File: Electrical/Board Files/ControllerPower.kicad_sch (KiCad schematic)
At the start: 42 parts, among them J1 Conn_01x02_Female, Q1 PJA3411, Q2 PJA3411, SW11 SW_DIP_x01, U1 TPS63020, U2 BQ25050DQCR

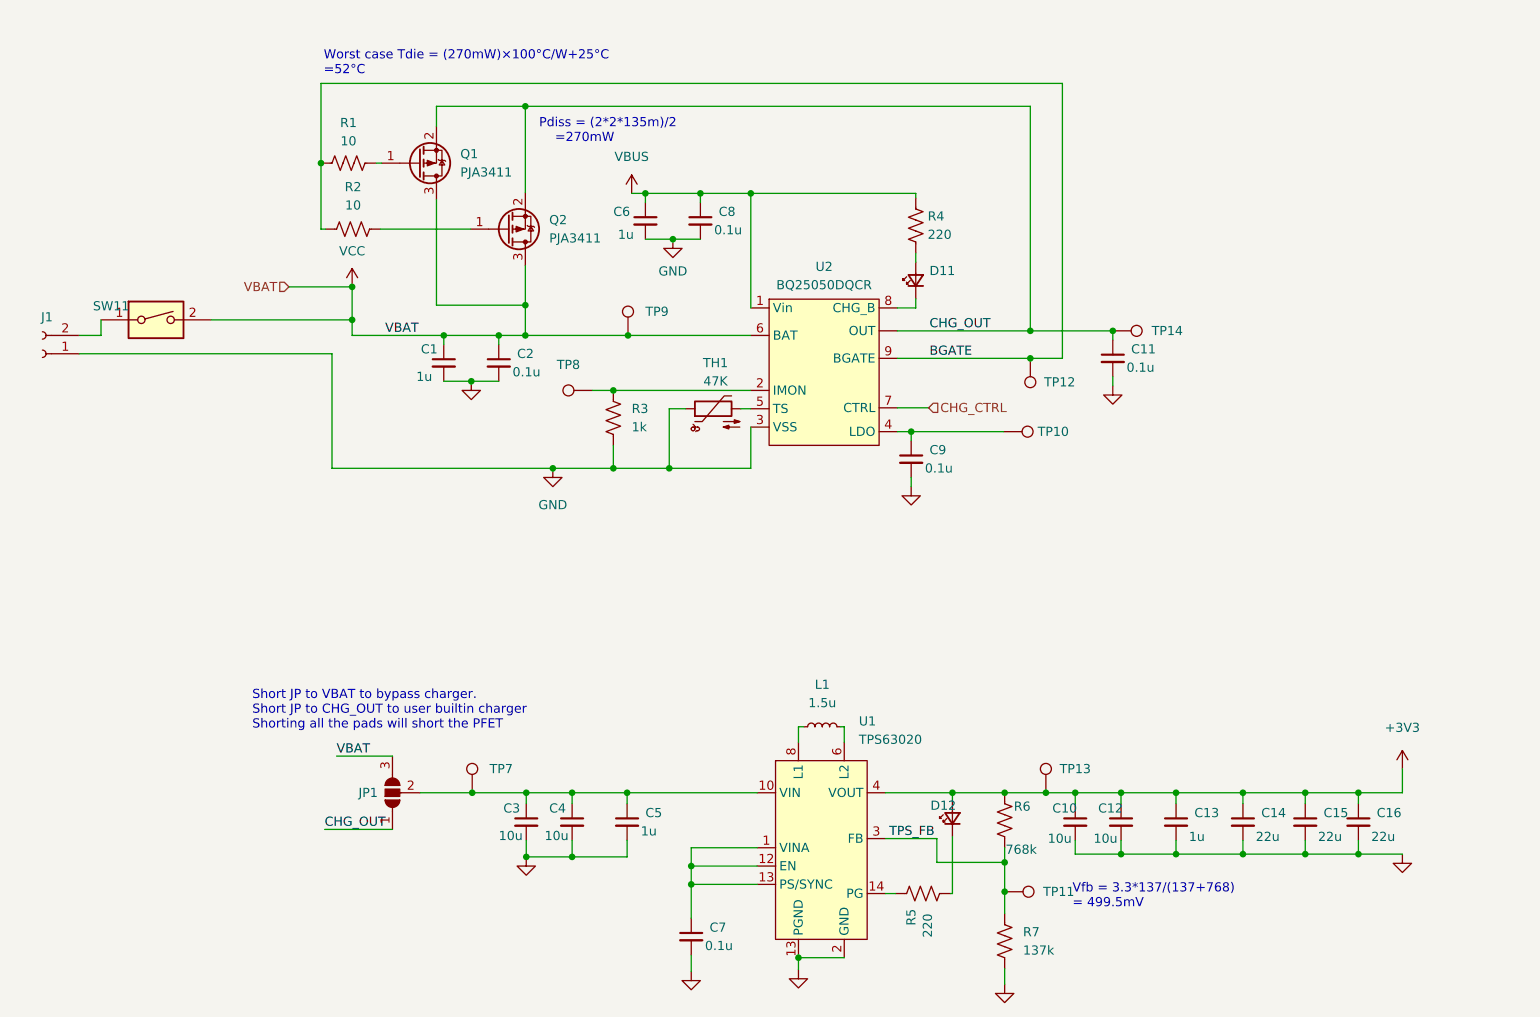
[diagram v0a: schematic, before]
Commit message: Added hall effect sensors
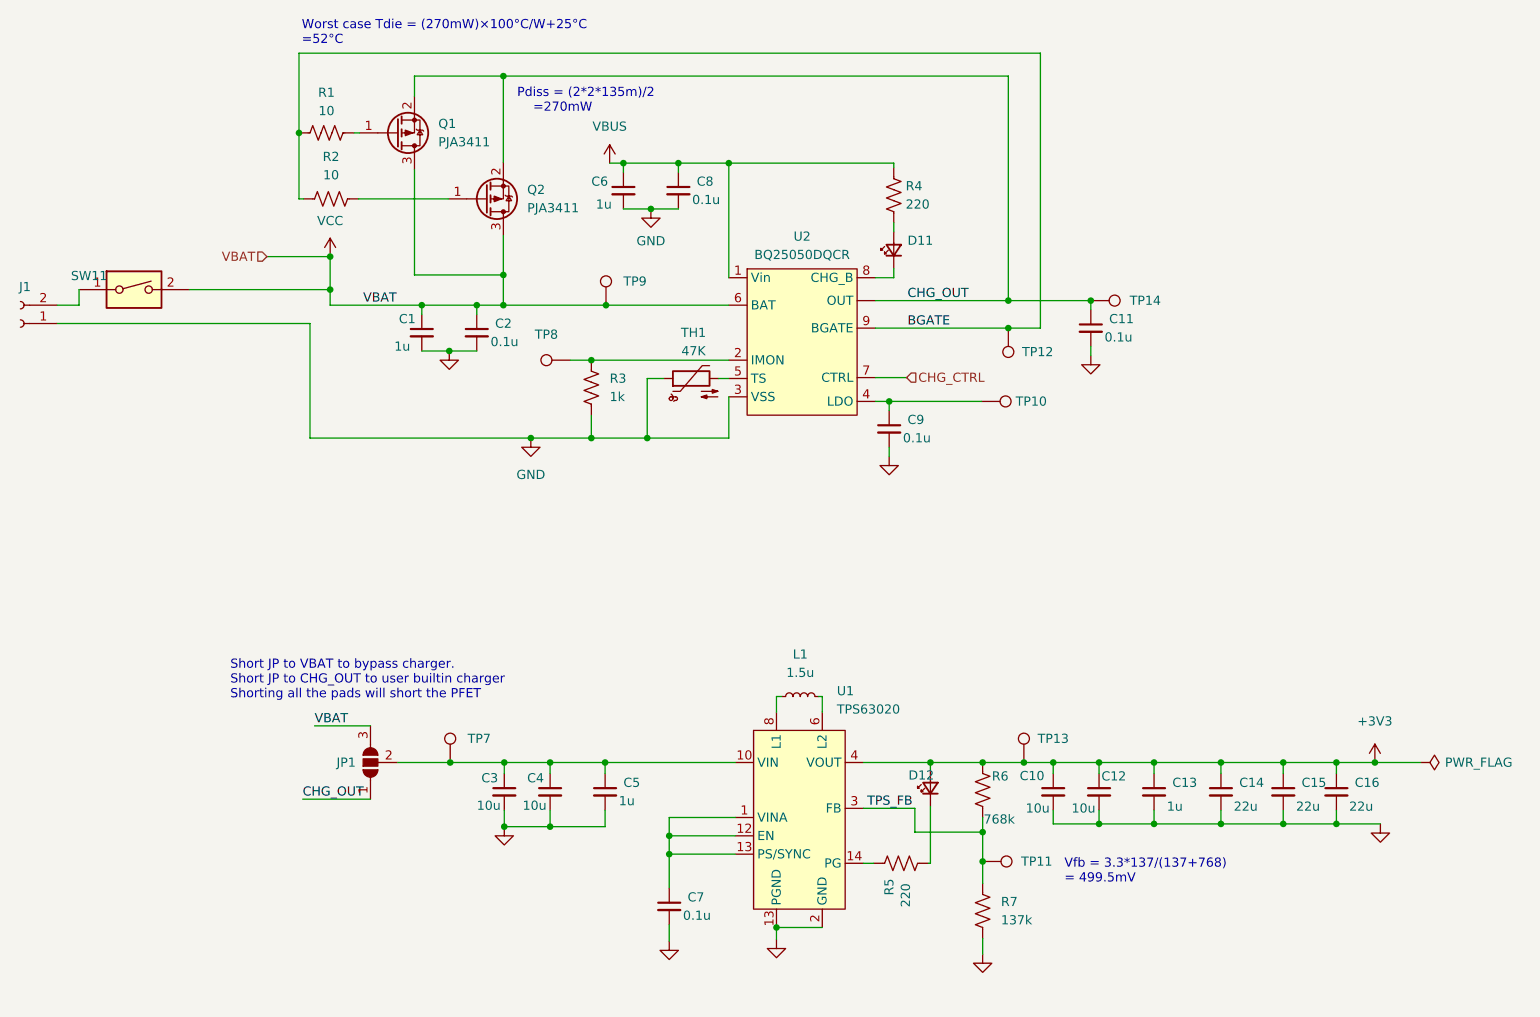
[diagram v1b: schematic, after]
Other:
- moved on the sheet: C1, C10, C11, C12, C13, C14, C15, C16, C2, C3, C4, C5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

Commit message: Updating title block fields and adding pdf schematic
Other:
- company: (none) -> Rockerbotics
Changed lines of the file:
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@@
   (title_block
     (title "Robotics Controller")
+    (date "2022-09-02")
     (rev "A")
+    (company "Rockerbotics")
   )
   (junction (at 189.738 56.388) (diameter 0) (color 0 0 0 0)
